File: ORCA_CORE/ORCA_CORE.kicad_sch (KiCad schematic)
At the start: 3 parts, among them J17 Vin_motor, J18 data_line_power, J19 +5Vin_cpu

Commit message: start making ORCA_CORE
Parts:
- added J23: motor_fork, symbol Connector_Generic:Conn_01x04
- added J24: motor_arm, symbol Connector_Generic:Conn_01x04
- added J25: servo_arm, symbol Connector_Generic:Conn_01x06
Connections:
- new net cpu_hat/IN_A_arm_out: J24.2 (Pin_2)
- new net cpu_hat/IN_A_fork_out: J23.2 (Pin_2)
- new net cpu_hat/IN_B_arm_out: J24.3 (Pin_3)
- new net cpu_hat/IN_B_fork_out: J23.3 (Pin_3)
- new net cpu_hat/motor_0_out: J25.2 (Pin_2)
- new net cpu_hat/motor_1_out: J25.3 (Pin_3)
- new net cpu_hat/motor_2_out: J25.4 (Pin_4)
- new net cpu_hat/motor_3_out: J25.5 (Pin_5)
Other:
- added sheet arm (arm.kicad_sch)
- added sheet cpu_hat (cpu_hat.kicad_sch)
- added sheet external_input (external_input.kicad_sch)
- added sheet md_arm (md.kicad_sch)
- added sheet md_fork (md.kicad_sch)
- sheet cpu ports: added 3V3_cpu, RXD_5V, SCL_cpu, SDA_cpu, TXD_5V, full_color_led; removed GND
- moved on the sheet: J17, J18, J19

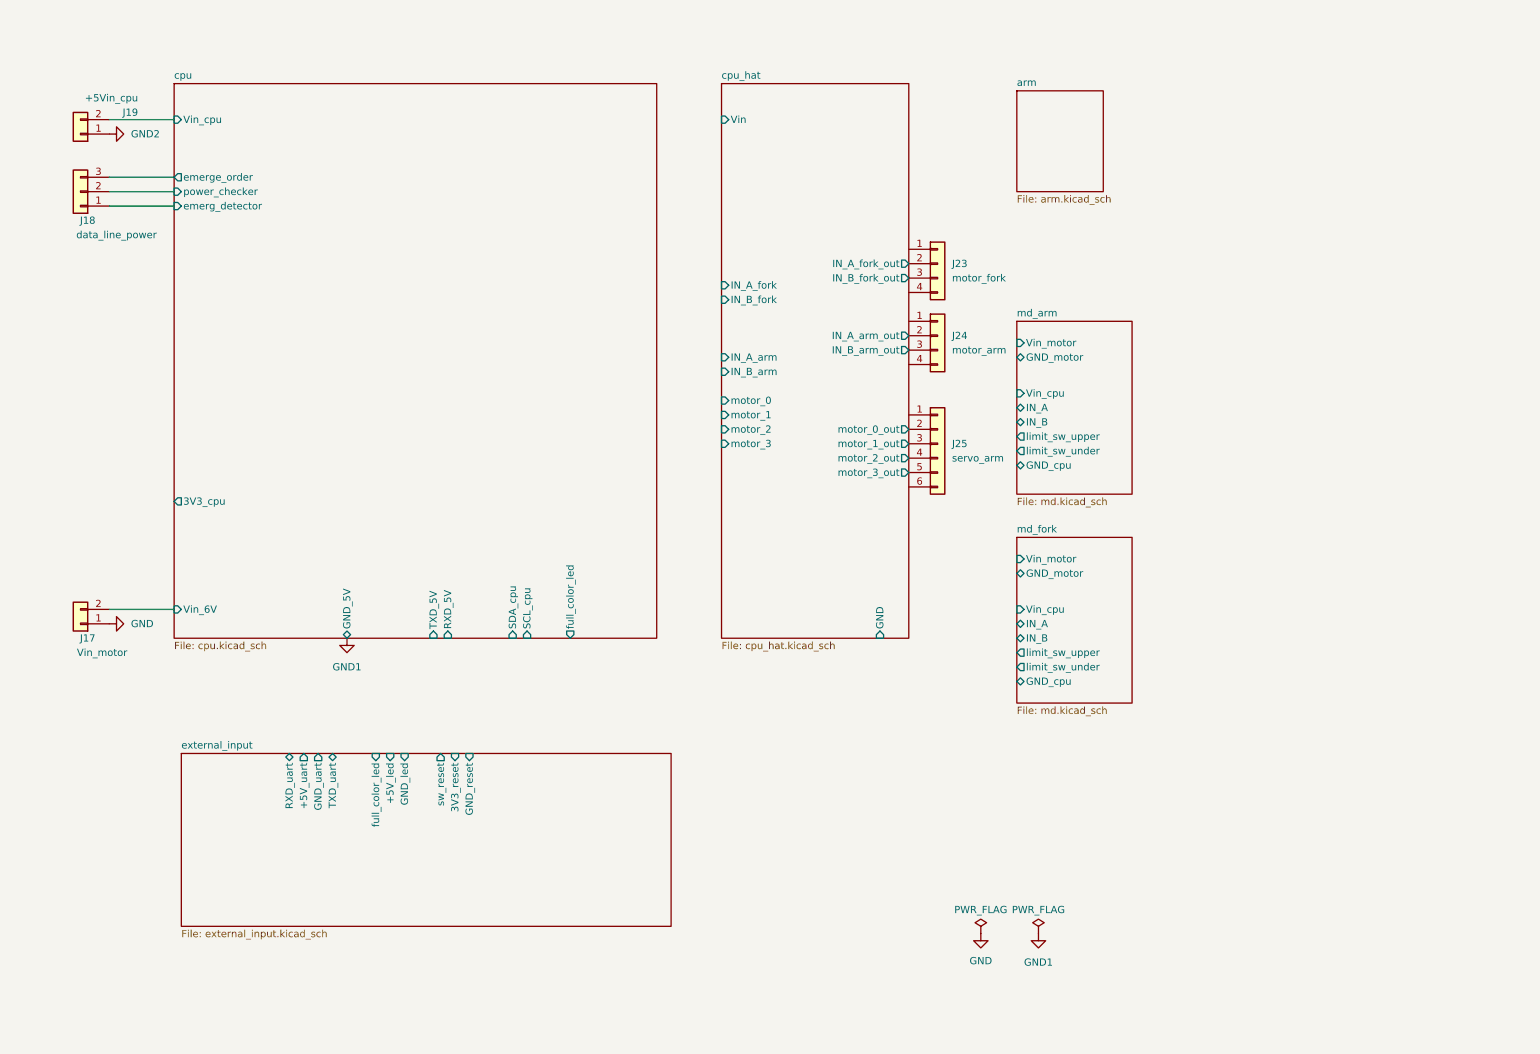
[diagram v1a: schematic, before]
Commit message: ordered power board
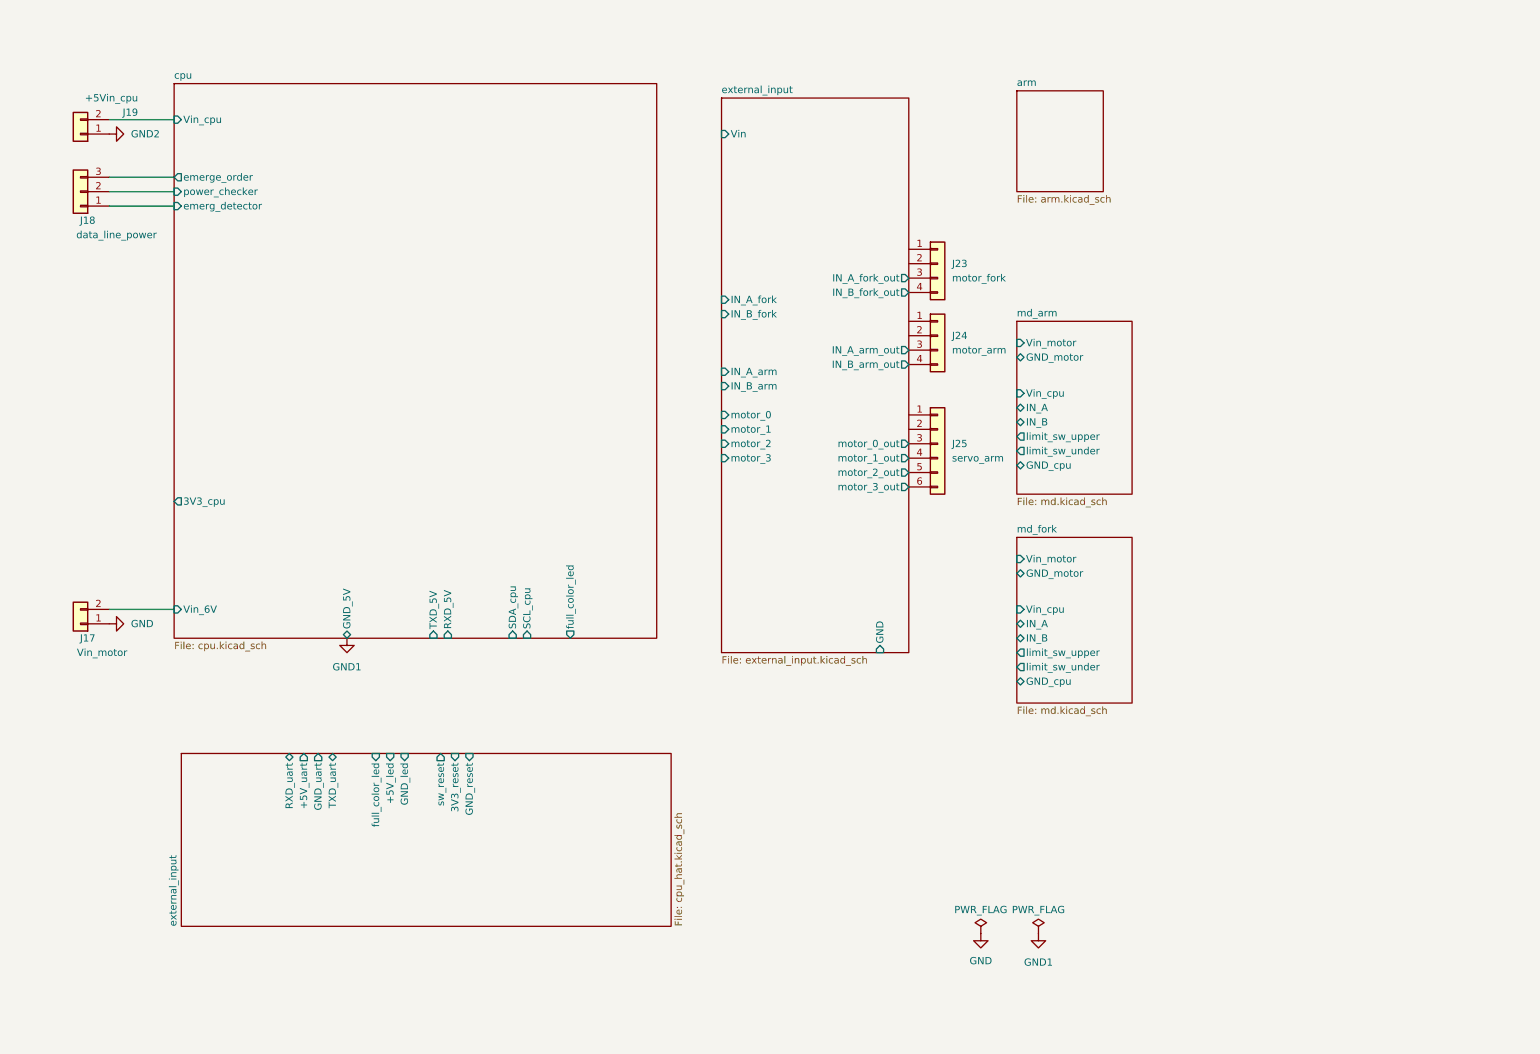
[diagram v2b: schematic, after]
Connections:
- net external_input/IN_B_arm_out: now reaches J24.4 (Pin_4)
- net external_input/motor_3_out: now reaches J25.6 (Pin_6)
- net external_input/IN_B_fork_out: now reaches J23.4 (Pin_4)
- net cpu_hat/IN_A_arm_out: no longer names the net of J24.2 (Pin_2)
- net cpu_hat/IN_A_fork_out: no longer names the net of J23.2 (Pin_2)
- net cpu_hat/IN_B_arm_out renamed external_input/IN_A_arm_out
- net cpu_hat/IN_B_fork_out renamed external_input/IN_A_fork_out
- net cpu_hat/motor_0_out: no longer names the net of J25.2 (Pin_2)
- net cpu_hat/motor_1_out renamed external_input/motor_0_out
- net cpu_hat/motor_2_out renamed external_input/motor_1_out
- net cpu_hat/motor_3_out renamed external_input/motor_2_out
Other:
- removed sheet cpu_hat
- sheet external_input ports: added GND, IN_A_arm, IN_A_arm_out, IN_A_fork, IN_A_fork_out, IN_B_arm, IN_B_arm_out, IN_B_fork, IN_B_fork_out, Vin, motor_0, motor_0_out, motor_1, motor_1_out, motor_2, motor_2_out, motor_3, motor_3_out; removed +5V_led, +5V_uart, 3V3_reset, GND_led, GND_reset, GND_uart, RXD_uart, TXD_uart, full_color_led, sw_reset
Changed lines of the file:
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@@
 		)
 		(property "Sheetname" "external_input"
-			(at 43.18 141.5284 0)
+			(at 42.4684 172.72 90)
 			(effects
 				(font
@@
 			)
 		)
-		(property "Sheetfile" "external_input.kicad_sch"
-			(at 43.18 173.3046 0)
+		(property "Sheetfile" "cpu_hat.kicad_sch"
+			(at 130.1246 172.72 90)
 			(effects
 				(font
@@
 	)
 	(sheet
-		(at 138.43 24.13)
+		(at 138.43 26.67)
 		(size 33.02 97.79)
 		(fields_autoplaced yes)
@@
 			(color 0 0 0 0.0000)
 		)
-		(property "Sheetname" "cpu_hat"
-			(at 138.43 23.4184 0)
+		(property "Sheetname" "external_input"
+			(at 138.43 25.9584 0)
 			(effects
 				(font
@@
 			)
 		)
-		(property "Sheetfile" "cpu_hat.kicad_sch"
-			(at 138.43 122.5046 0)
+		(property "Sheetfile" "external_input.kicad_sch"
+			(at 138.43 125.0446 0)
 			(effects
 				(font
@@
 			)
 		)
+		(property "フィールド2" ""
+			(at 138.43 26.67 0)
+			(effects
+				(font
+					(size 1.27 1.27)
+				)
+				(hide yes)
+			)
+		)
 		(pin "IN_B_fork" input
+			(at 138.43 64.77 180)
+			(effects
+				(font
+					(size 1.27 1.27)
+				)
+				(justify left)
+			)
+		)
+		(pin "IN_B_fork_out" output
+			(at 171.45 60.96 0)
+			(effects
+				(font
+					(size 1.27 1.27)
+				)
+				(justify right)
+			)
+		)
+		(pin "IN_A_fork" input
 			(at 138.43 62.23 180)
 			(effects
@@
 			)
 		)
-		(pin "IN_B_fork_out" output
+		(pin "IN_A_arm" input
+			(at 138.43 74.93 180)
+			(effects
+				(font
+					(size 1.27 1.27)
+				)
+				(justify left)
+			)
+		)
+		(pin "IN_B_arm" input
+			(at 138.43 77.47 180)
+			(effects
+				(font
+					(size 1.27 1.27)
+				)
+				(justify left)
+			)
+		)
+		(pin "IN_B_arm_out" output
+			(at 171.45 73.66 0)
+			(effects
+				(font
+					(size 1.27 1.27)
+				)
+				(justify right)
+			)
+		)
+		(pin "IN_A_arm_out" output
+			(at 171.45 71.12 0)
+			(effects
+				(font
+					(size 1.27 1.27)
+				)
+				(justify right)
+			)
+		)
+		(pin "motor_1_out" output
+			(at 171.45 90.17 0)
+			(effects
+				(font
+					(size 1.27 1.27)
+				)
+				(justify right)
+			)
+		)
+		(pin "motor_3" input
+			(at 138.43 90.17 180)
+			(effects
+				(font
+					(size 1.27 1.27)
+				)
+				(justify left)
+			)
+		)
+		(pin "motor_0_out" output
+			(at 171.45 87.63 0)
+			(effects
+				(font
+					(size 1.27 1.27)
+				)
+				(justify right)
+			)
+		)
+		(pin "motor_1" input
+			(at 138.43 85.09 180)
+			(effects
+				(font
+					(size 1.27 1.27)
+				)
+				(justify left)
+			)
+		)
+		(pin "motor_0" input
+			(at 138.43 82.55 180)
+			(effects
+				(font
+					(size 1.27 1.27)
+				)
+				(justify left)
+			)
+		)
+		(pin "motor_2" input
+			(at 138.43 87.63 180)
+			(effects
+				(font
+					(size 1.27 1.27)
+				)
+				(justify left)
+			)
+		)
+		(pin "IN_A_fork_out" output
 			(at 171.45 58.42 0)
 			(effects
@@
 			)
 		)
-		(pin "IN_A_fork" input
-			(at 138.43 59.69 180)
-			(effects
-				(font
-					(size 1.27 1.27)
-				)
-				(justify left)
-			)
-		)
-		(pin "IN_A_arm" input
-			(at 138.43 72.39 180)
-			(effects
-				(font
-					(size 1.27 1.27)
-				)
-				(justify left)
-			)
-		)
-		(pin "IN_B_arm" input
-			(at 138.43 74.93 180)
-			(effects
-				(font
-					(size 1.27 1.27)
-				)
-				(justify left)
-			)
-		)
-		(pin "IN_B_arm_out" output
-			(at 171.45 71.12 0)
-			(effects
-				(font
-					(size 1.27 1.27)
-				)
-				(justify right)
-			)
-		)
-		(pin "IN_A_arm_out" output
-			(at 171.45 68.58 0)
-			(effects
-				(font
-					(size 1.27 1.27)
-				)
-				(justify right)
-			)
-		)
-		(pin "motor_1_out" output
-			(at 171.45 87.63 0)
-			(effects
-				(font
-					(size 1.27 1.27)
-				)
-				(justify right)
-			)
-		)
-		(pin "motor_3" input
-			(at 138.43 87.63 180)
-			(effects
-				(font
-					(size 1.27 1.27)
-				)
-				(justify left)
-			)
-		)
-		(pin "motor_0_out" output
-			(at 171.45 85.09 0)
-			(effects
-				(font
-					(size 1.27 1.27)
-				)
-				(justify right)
-			)
-		)
-		(pin "motor_1" input
-			(at 138.43 82.55 180)
-			(effects
-				(font
-					(size 1.27 1.27)
-				)
-				(justify left)
-			)
-		)
-		(pin "motor_0" input
-			(at 138.43 80.01 180)
-			(effects
-				(font
-					(size 1.27 1.27)
-				)
-				(justify left)
-			)
-		)
-		(pin "motor_2" input
-			(at 138.43 85.09 180)
-			(effects
-				(font
-					(size 1.27 1.27)
-				)
-				(justify left)
-			)
-		)
-		(pin "IN_A_fork_out" output
-			(at 171.45 55.88 0)
-			(effects
-				(font
-					(size 1.27 1.27)
-				)
-				(justify right)
-			)
-		)
 		(pin "GND" input
-			(at 166.37 121.92 270)
+			(at 166.37 124.46 270)
 			(effects
 				(font
@@
 		)
 		(pin "Vin" input
-			(at 138.43 30.48 180)
+			(at 138.43 33.02 180)
 			(effects
 				(font
@@
 		)
 		(pin "motor_2_out" output
-			(at 171.45 90.17 0)
+			(at 171.45 92.71 0)
 			(effects
 				(font
@@
 		)
 		(pin "motor_3_out" output
-			(at 171.45 92.71 0)
-			(effects
-				(font
+			(at 171.45 95.25 0)
+			(effects
+				(font

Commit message: add power registers to power_board gate driver
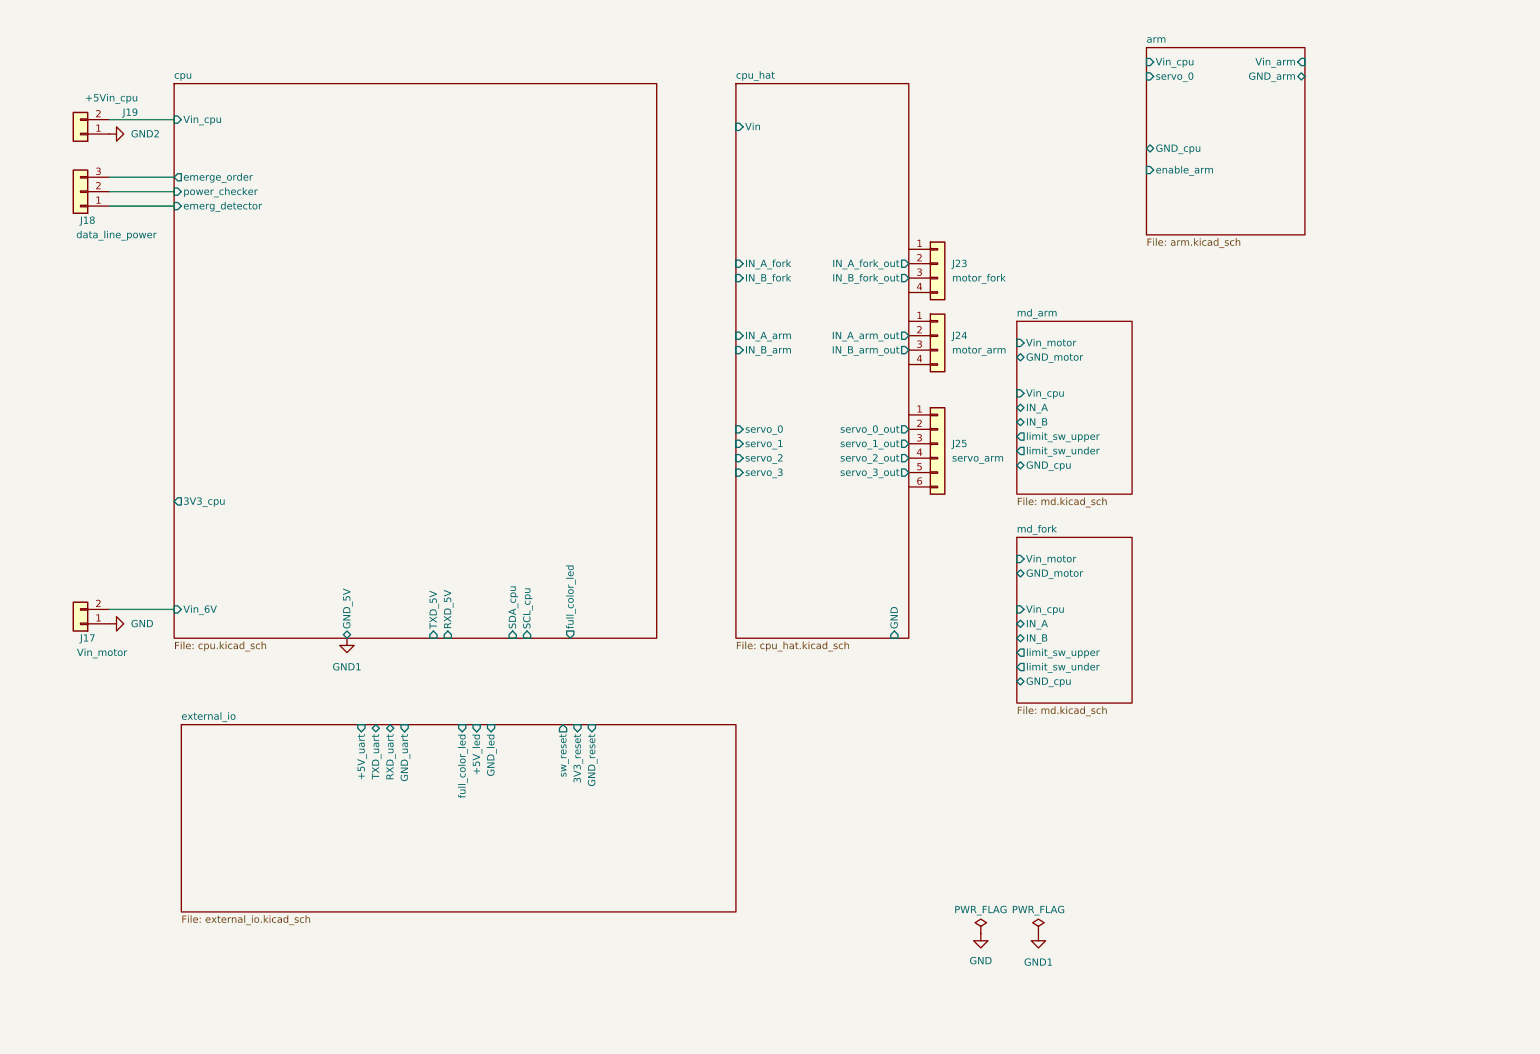
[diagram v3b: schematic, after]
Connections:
- net cpu_hat/IN_A_arm_out: now reaches J24.2 (Pin_2)
- net cpu_hat/servo_0_out: now reaches J25.2 (Pin_2)
- net cpu_hat/IN_A_fork_out: now reaches J23.2 (Pin_2)
- net external_io/IN_A_arm_out renamed cpu_hat/IN_B_arm_out
- net external_io/IN_A_fork_out renamed cpu_hat/IN_B_fork_out
- net external_io/IN_B_arm_out: no longer names the net of J24.4 (Pin_4)
- net external_io/IN_B_fork_out: no longer names the net of J23.4 (Pin_4)
- net external_io/motor_0_out renamed cpu_hat/servo_1_out
- net external_io/motor_1_out renamed cpu_hat/servo_2_out
- net external_io/motor_2_out renamed cpu_hat/servo_3_out
- net external_io/motor_3_out: no longer names the net of J25.6 (Pin_6)
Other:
- sheet external_input renamed external_io
- added sheet cpu_hat (cpu_hat.kicad_sch)
- sheet arm ports: added GND_arm, GND_cpu, Vin_arm, Vin_cpu, enable_arm, servo_0; removed none
- sheet external_io: file external_input.kicad_sch -> external_io.kicad_sch
- sheet external_io ports: added +5V_led, +5V_uart, 3V3_reset, GND_led, GND_reset, GND_uart, RXD_uart, TXD_uart, full_color_led, sw_reset; removed GND, IN_A_arm, IN_A_arm_out, IN_A_fork, IN_A_fork_out, IN_B_arm, IN_B_arm_out, IN_B_fork, IN_B_fork_out, Vin, motor_0, motor_0_out, motor_1, motor_1_out, motor_2, motor_2_out, motor_3, motor_3_out

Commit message: almost completed CORE
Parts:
- removed J17: Vin_motor, Conn:power_pad, symbol Connector_Generic:Conn_01x02
- removed J18: data_line_power, Connector_JST:JST_XH_B3B-XH-A_1x03_P2.50mm_Vertical, symbol Connector_Generic:Conn_01x03
- removed J23: motor_fork, symbol Connector_Generic:Conn_01x04
- removed J24: motor_arm, symbol Connector_Generic:Conn_01x04
- added J18: +3V3_motor, Conn:power_pad, symbol Connector_Generic:Conn_01x02
- added J23, J39: md_arm, symbol Connector_Generic:Conn_01x06
- added J24, J40: md_fork, symbol Connector_Generic:Conn_01x06
- added J34, J36: cpu_male_1, Connector_PinHeader_2.54mm:PinHeader_2x10_P2.54mm_Vertical, symbol Connector_Generic:Conn_02x10_Odd_Even
- added J35, J37: hat_female_1, Connector_PinHeader_2.54mm:PinHeader_2x10_P2.54mm_Vertical, symbol Connector_Generic:Conn_02x10_Odd_Even
- added J38: servo_arm, symbol Connector_Generic:Conn_01x06
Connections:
- net GND2 is gone; now on net GND1: J19.1 (Pin_1)
- net GND: now also J18.1 (Pin_1)
- net GND1: now also J25.1 (Pin_1), J23.1 (Pin_1), J24.1 (Pin_1)
- net arm/GND_cpu: now also J38.1 (Pin_1)
- net arm/Vin_cpu: now also J38.6 (Pin_6)
- net arm/servo_0: now also J38.2 (Pin_2)
- net cpu_hat/IN_A_arm_out: now also J24.2 (Pin_2)
- net cpu_hat/IN_A_fork_out: now also J23.2 (Pin_2)
- net cpu_hat/IN_B_arm_out: now also J24.3 (Pin_3)
- net cpu_hat/IN_B_fork_out: now also J23.3 (Pin_3)
- net md_arm/GND_cpu: now also J39.1 (Pin_1)
- net md_arm/IN_A: now also J39.2 (Pin_2)
- net md_arm/IN_B: now also J39.3 (Pin_3)
- net md_arm/Vin_cpu: now also J39.6 (Pin_6)
- net md_arm/limit_sw_under: now also J39.5 (Pin_5)
- net md_arm/limit_sw_upper: now also J39.4 (Pin_4)
- net md_fork/GND_cpu: now also J40.1 (Pin_1)
- net md_fork/IN_A: now also J40.2 (Pin_2)
- net md_fork/IN_B: now also J40.3 (Pin_3)
- net md_fork/Vin_cpu: now also J40.6 (Pin_6)
- net md_fork/limit_sw_under: now also J40.5 (Pin_5)
- net md_fork/limit_sw_upper: now also J40.4 (Pin_4)
- net +3V3: now reaches J25.6 (Pin_6)
- net +3V3: now also J23.6 (Pin_6), J24.6 (Pin_6)
- new net arm/servo_1: J38.3 (Pin_3)
- new net arm/servo_2: J38.4 (Pin_4)
- new net arm/servo_3: J38.5 (Pin_5)
- new net cpu/3V3_motor: J18.2 (Pin_2)
- new net cpu_hat/limit_sw_under_arm_in: J23.5 (Pin_5)
- new net cpu_hat/limit_sw_under_fork_in: J24.5 (Pin_5)
- new net cpu_hat/limit_sw_upper_arm_in: J23.4 (Pin_4)
- new net cpu_hat/limit_sw_upper_fork_in: J24.4 (Pin_4)
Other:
- sheet arm ports: added servo_1, servo_2, servo_3; removed none
- sheet cpu ports: added 3V3_motor, GND_cpu, GND_motor, INA_arm, INA_fork, INB_arm, INB_fork, Vout_cpu, enable_arm, led, limit_sw_under_arm, limit_sw_under_fork, limit_sw_upper_arm, limit_sw_upper_fork, rest, servo_0, servo_1, servo_2, servo_3, servo_camera; removed GND_5V, Vin_6V, full_color_led
- sheet cpu_hat ports: added RX, RX_out, SCL, SDA, TX, TX_out, Vin_3V3, emerge_detector, emerge_order, enable_arm, enable_arm_out, led, led_out, limit_sw_under_arm, limit_sw_under_arm_in, limit_sw_under_fork, limit_sw_under_fork_in, limit_sw_upper_arm, limit_sw_upper_arm_in, limit_sw_upper_fork, limit_sw_upper_fork_in, power_checker, reset, reset_out, seervo_camera, seervo_camera_out; removed none
- moved on the sheet: J19, J25
